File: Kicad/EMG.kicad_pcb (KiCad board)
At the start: 2 copper layers, 50 x 35 mm, 46 parts, among them IC1 MAX8881EUT33-T, P1 nRF24l01, P2 CONN_01X02, P3 USB_A, P4 CONN_01X05, P5 CONN_01X03, SW1 SW_PUSH, U1 MSP430G2231IPW14, U2 TLC2274, U3 TLC2274, U4 MCP73831

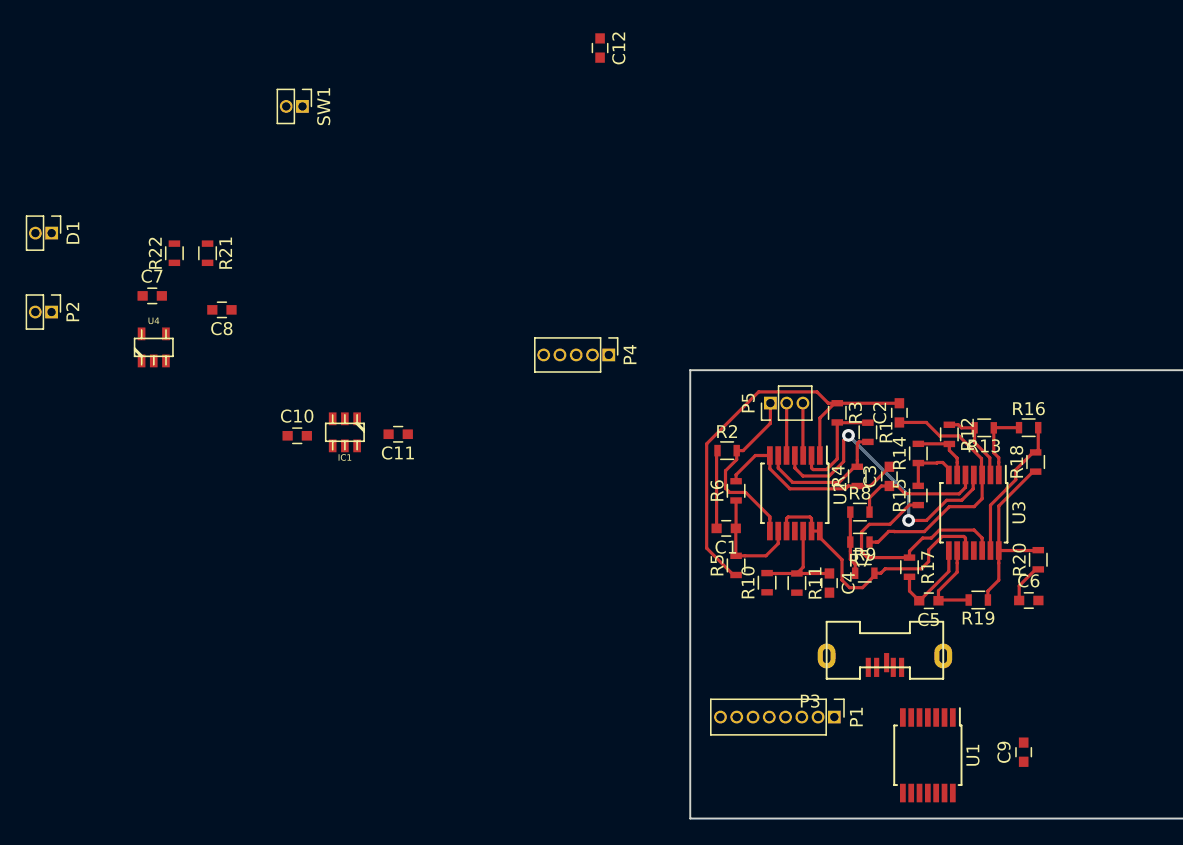
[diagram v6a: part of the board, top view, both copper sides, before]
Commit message: Ruteo. Falta conectar GND
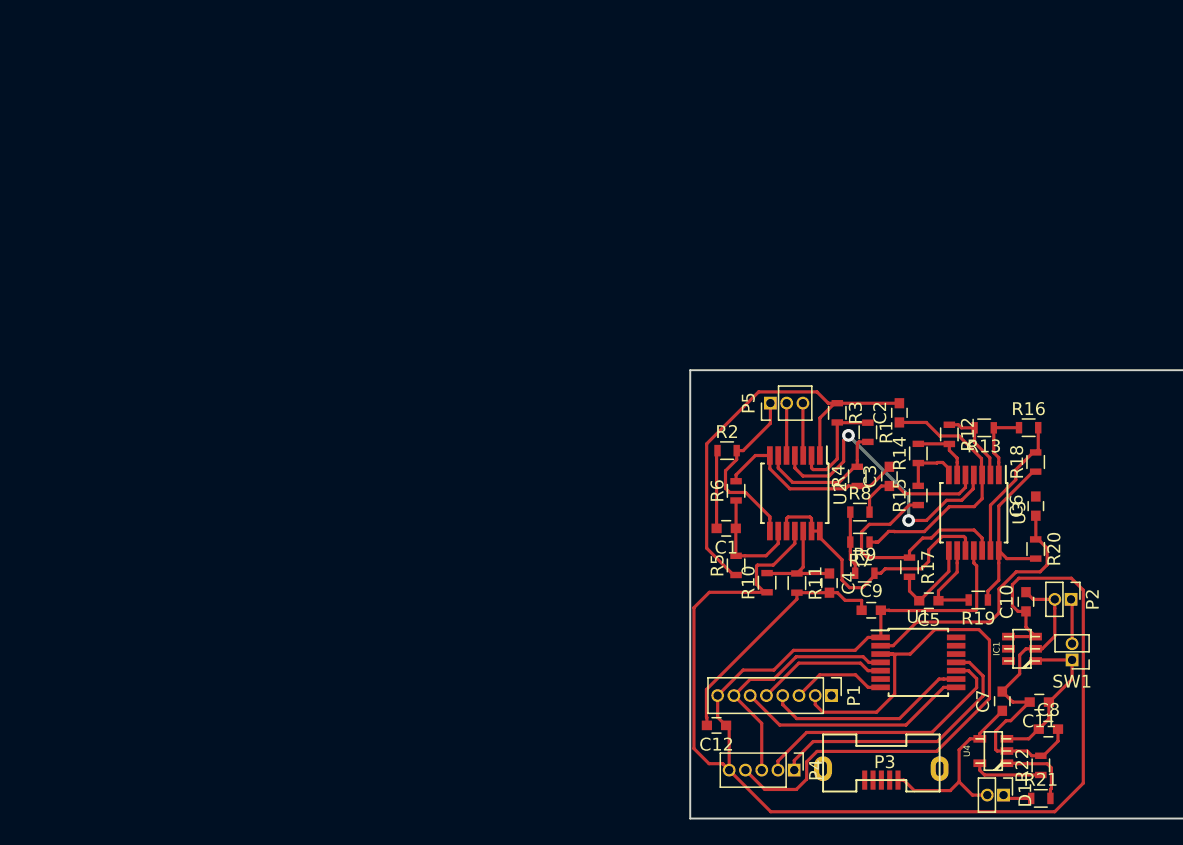
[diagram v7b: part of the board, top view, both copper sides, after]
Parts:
- moved D1 86.3 mm to (164.8, 152.3)
- moved P2 82.7 mm to (170.1, 137.0)
- moved R22 78.6 mm to (167.7, 150.0)
- moved R21 77.7 mm to (167.7, 152.6), turned to 0 degrees
- moved SW1 74.0 mm to (170.2, 141.7), turned to 180 degrees
- moved C7 73.5 mm to (164.7, 145.0), turned to 90 degrees
- moved U4 72.7 mm to (164.0, 148.8), turned to 90 degrees
- moved C8 72.3 mm to (168.3, 147.1), turned to 0 degrees
- moved C10 58.3 mm to (166.6, 137.2), turned to 90 degrees
- moved IC1 55.5 mm to (166.2, 140.9), turned to 90 degrees
- moved C11 54.2 mm to (167.6, 145.0)
- moved C12 53.7 mm to (142.4, 146.8), turned to 180 degrees
- moved P4 35.5 mm to (148.5, 150.3)
- moved C9 16.3 mm to (154.5, 137.9), turned to 0 degrees
- moved P3 8.80 mm to (155.3, 151.1)
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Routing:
- net VCC: track 0.00 -> 121.6 mm
- net /Microcontrolador/CE: track 0.00 -> 48.7 mm
- net GND: track 23.5 -> 68.9 mm
- net TEST: track 0.00 -> 21.7 mm
- net RST: track 0.00 -> 21.1 mm
- net /Microcontrolador/CSN: track 0.00 -> 19.6 mm
- net /Microcontrolador/MOSI: track 0.00 -> 18.3 mm
- net /Microcontrolador/ADCin: track 3.16 -> 21.0 mm
- net /Microcontrolador/MISO: track 0.00 -> 16.0 mm
- net Net-(C7-Pad1): track 0.00 -> 15.8 mm
- net +BATT: track 0.00 -> 12.2 mm
- net /Microcontrolador/IRQ: track 0.00 -> 10.2 mm
- net /Microcontrolador/SCK: track 0.00 -> 7.44 mm
- net Net-(R21-Pad2): track 0.00 -> 6.04 mm
- net Net-(R22-Pad1): track 0.00 -> 5.47 mm
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
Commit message: Finalizada primera versión del pcb.
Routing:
- net GND: track 68.9 -> 126.4 mm, vias 2 -> 12
- added copper zone on F.Cu, net GND
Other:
- board size 50 x 35 mm -> 32 x 35 mm
